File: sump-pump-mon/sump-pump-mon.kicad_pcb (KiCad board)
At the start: 2 copper layers, 36 parts, among them J1 Main Input, J2 Wall Power, J3 Battery, J4 Conn_01x06_Pin, J5 Aux Input, SW3 MODE, SW4 POWER, U1 L7805, U2 4N25, U3 4N25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

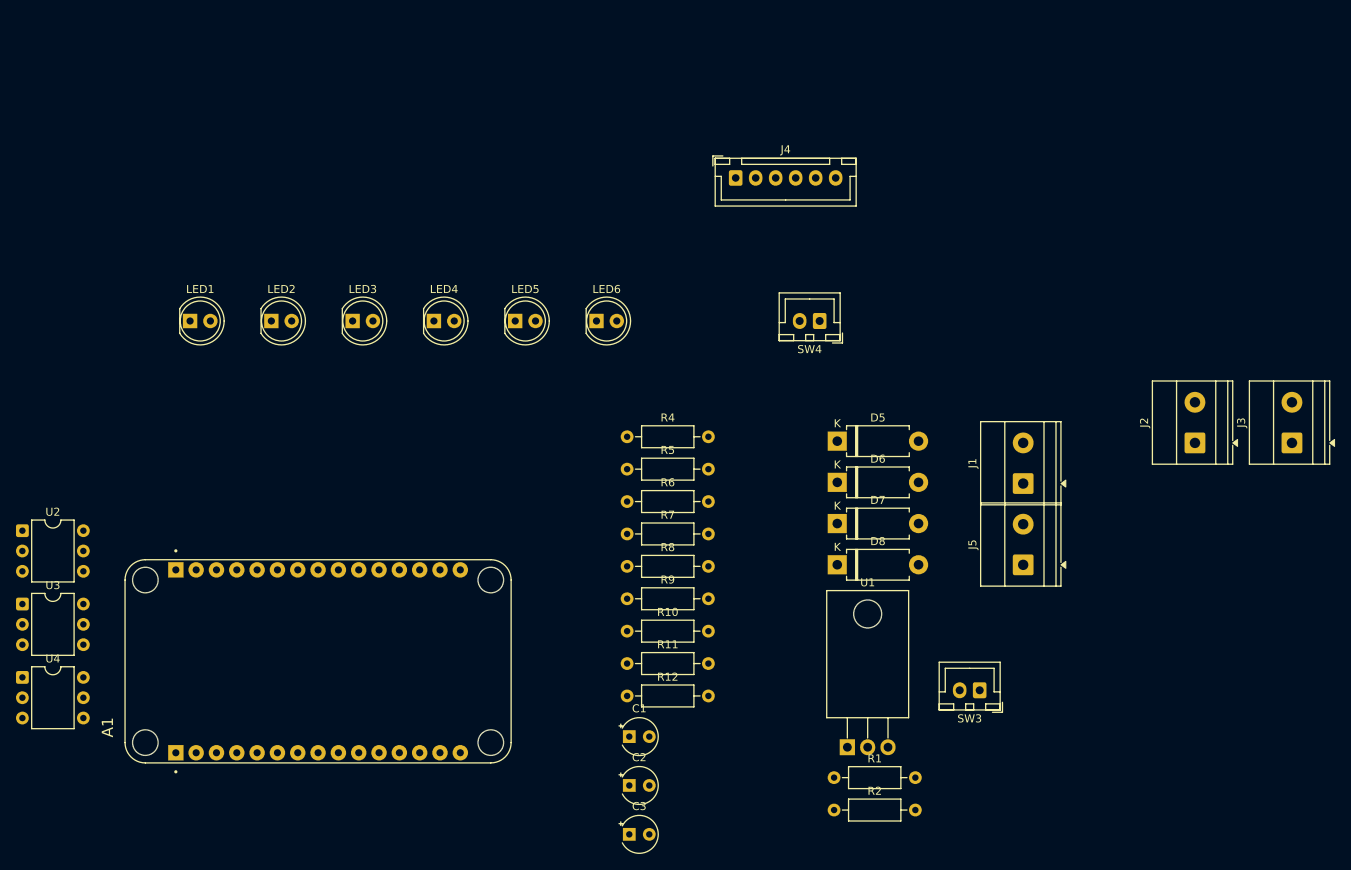
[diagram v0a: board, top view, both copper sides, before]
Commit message: Rough parts placement and partial routing
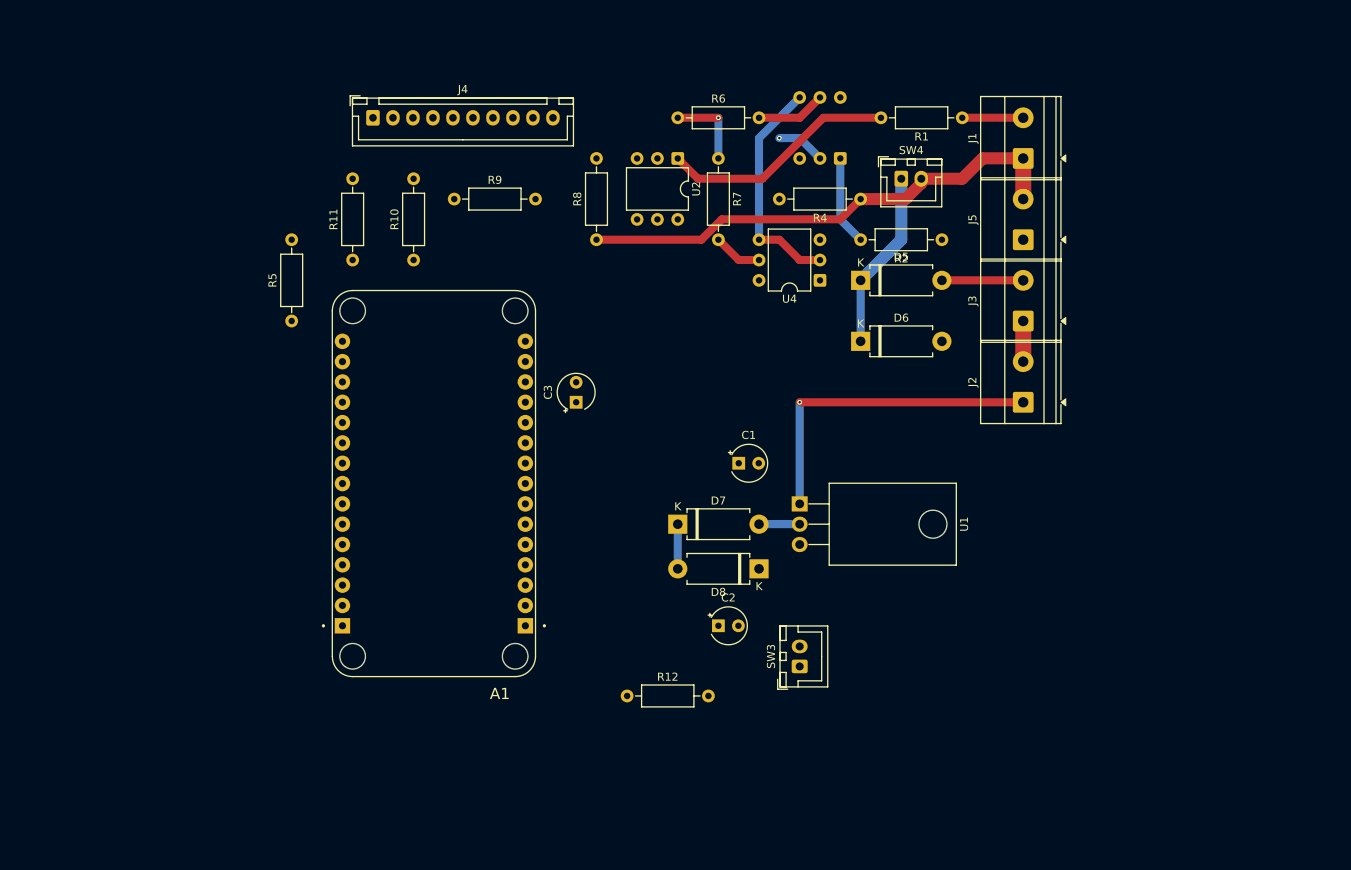
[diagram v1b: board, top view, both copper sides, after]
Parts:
- removed LED1: LED_POWER, LED_THT:LED_D5.0mm
- removed LED2: LED_MAIN, LED_THT:LED_D5.0mm
- removed LED3: LED_AUX, LED_THT:LED_D5.0mm
- removed LED4: GREEN, LED_THT:LED_D5.0mm
- removed LED5: YELLOW, LED_THT:LED_D5.0mm
- removed LED6: LED_MODE, LED_THT:LED_D5.0mm
- J4: footprint Connector_JST:JST_XH_B6B-XH-A_1x06_P2.50mm_Vertical -> Connector_JST:JST_XH_B10B-XH-A_1x10_P2.50mm_Vertical
- U3: moved to B.Cu
- moved U3 116.4 mm to (195.6, 35.6), turned to 90 degrees
- moved U4 111.4 mm to (193.0, 50.8), turned to 180 degrees
- moved U2 94.2 mm to (175.3, 35.6), turned to -90 degrees
- moved R1 84.0 mm to (210.8, 30.5), turned to 180 degrees
- moved R2 72.6 mm to (208.3, 45.7), turned to 180 degrees
- moved R11 61.0 mm to (134.6, 48.3), turned to 90 degrees
- moved R9 54.4 mm to (147.3, 40.6)
- moved C3 54.4 mm to (162.6, 66.0), turned to 90 degrees
- moved R10 53.5 mm to (142.2, 48.3), turned to 90 degrees
- moved R6 48.4 mm to (175.3, 30.5)
- moved R7 48.3 mm to (180.3, 35.6), turned to -90 degrees
- moved J4 46.0 mm to (137.2, 30.5)
- moved R5 45.8 mm to (127.0, 55.9), turned to 90 degrees
- moved R4 41.7 mm to (198.1, 40.6), turned to 180 degrees
- moved R8 41.0 mm to (165.1, 45.7), turned to 90 degrees
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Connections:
- C1 pad 1: Net-(J2-Pin_2) -> Net-(J2-Pin_1)
- J2 pad 1: GND -> Net-(J2-Pin_1)
- J2 pad 2: Net-(J2-Pin_2) -> GND
- J4 pad 6: GND -> LED_AUX
- R1 pad 2: Net-(LED2-A) -> Net-(R1-Pad2)
- R2 pad 2: Net-(LED3-A) -> Net-(R2-Pad2)
- U1 pad 1: Net-(J2-Pin_2) -> Net-(J2-Pin_1)
- U2 pad 1: Net-(LED2-K) -> Net-(R1-Pad2)
- U2 pad 2: GND -> LED_MAIN
- U3 pad 1: Net-(LED3-K) -> Net-(R2-Pad2)
- U3 pad 2: GND -> LED_AUX
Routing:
- net Vin: track 0.00 -> 63.0 mm
- net Net-(J2-Pin_1): track 0.00 -> 40.6 mm, vias 0 -> 1
- net GND: track 0.00 -> 33.6 mm
- net Net-(R1-Pad2): track 0.00 -> 29.6 mm
- net Net-(D5-K): track 0.00 -> 22.4 mm
- net Net-(R2-Pad2): track 0.00 -> 11.2 mm
- net +3.3V: track 0.00 -> 10.2 mm, vias 0 -> 1
- net Net-(D5-A): track 0.00 -> 10.2 mm
- net Aux_Input: track 0.00 -> 8.67 mm
- net Net-(J1-Pin_2): track 0.00 -> 7.62 mm
- net Power_Failure: track 0.00 -> 6.13 mm
- net LED_AUX: track 0.00 -> 6.13 mm, vias 0 -> 1
- net Net-(D7-K): track 0.00 -> 5.58 mm
- net Net-(D7-A): track 0.00 -> 5.08 mm

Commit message: Routing complete
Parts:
- added H1: MountingHole, MountingHole:MountingHole_3.7mm, F.Cu at (218.4, 22.9)
- added H2: MountingHole, MountingHole:MountingHole_3.7mm, F.Cu at (218.4, 73.7)
- added H3: MountingHole, MountingHole:MountingHole_3.7mm, F.Cu at (116.4, 22.9)
- added H4: MountingHole, MountingHole:MountingHole_3.7mm, F.Cu at (116.4, 73.7)
- added J6: I2C, Connector_JST:JST_XH_B2B-XH-A_1x02_P2.50mm_Vertical, F.Cu at (135.9, 24.1)
- added R13: 2.7k, Resistor_THT:R_Axial_DIN0207_L6.3mm_D2.5mm_P10.16mm_Horizontal, F.Cu at (153.7, 21.6)
- added R14: 2.7k, Resistor_THT:R_Axial_DIN0207_L6.3mm_D2.5mm_P10.16mm_Horizontal, F.Cu at (116.8, 50.8)
- J2, J3: footprint TerminalBlock_Phoenix:TerminalBlock_Phoenix_MKDS-1,5-2-5.08_1x02_P5.08mm_Horizontal -> Connector_JST:JST_XH_B2B-XH-A_1x02_P2.50mm_Vertical
- J4: value Conn_01x06_Pin -> Display_Conn; footprint Connector_JST:JST_XH_B10B-XH-A_1x10_P2.50mm_Vertical -> Connector_JST:JST_XH_B12B-XH-A_1x12_P2.50mm_Vertical
- U1: footprint Package_TO_SOT_THT:TO-220-3_Horizontal_TabDown -> Package_TO_SOT_THT:TO-220-3_Vertical
- U3: moved to F.Cu
- moved SW3 51.4 mm to (172.7, 50.8), turned to 0 degrees
- moved C3 46.4 mm to (116.8, 58.4), turned to 0 degrees
- moved J4 36.8 mm to (163.8, 55.9), turned to 90 degrees
- moved R12 35.7 mm to (152.4, 71.1), turned to 90 degrees
- moved R5 32.1 mm to (157.5, 66.0)
- moved C2 31.8 mm to (195.6, 66.0), turned to 90 degrees
- moved D8 28.9 mm to (190.5, 58.4)
- moved A1 25.0 mm to (134.6, 53.3), turned to 0 degrees
- moved C1 21.7 mm to (203.2, 66.0), turned to 90 degrees
- moved R11 20.5 mm to (152.4, 58.4)
- moved D7 16.1 mm to (180.3, 66.0)
- moved U1 14.8 mm to (203.2, 71.1), turned to 180 degrees
- moved R8 10.8 mm to (157.5, 53.3)
- moved R10 10.5 mm to (152.4, 45.7)
- moved R9 10.2 mm to (157.5, 40.6), turned to 90 degrees
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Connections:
- net LED_POWER renamed LED_6V
- A1 pad J1_11: Net-(A1A-3V3) -> +3.3V
- A1 pad J2_4: unconnected-(A1B-D3-PadJ2_4) -> Net-(A1B-D3)
- A1 pad J2_5: unconnected-(A1B-D4-PadJ2_5) -> Net-(A1B-D4)
- C3 pad 1: Net-(A1A-3V3) -> +3.3V
- R10 pad 1: Net-(A1B-D2) -> Net-(A1B-D4)
- R9 pad 1: Net-(A1B-D1) -> Net-(A1B-D3)
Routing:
- net GND: track 33.6 -> 204.2 mm, vias 0 -> 1
- net +3.3V: track 10.2 -> 139.8 mm
- net Vin: track 63.0 -> 191.0 mm, vias 0 -> 2
- net Power_Failure: track 6.13 -> 69.4 mm, vias 0 -> 2
- net Aux_Input: track 8.67 -> 66.8 mm, vias 0 -> 1
- net Net-(A1B-D2): track 0.00 -> 53.3 mm
- net Mode: track 0.00 -> 46.8 mm, vias 0 -> 1
- net LED_AUX: track 6.13 -> 46.4 mm
- net Main_Input: track 0.00 -> 37.9 mm, vias 0 -> 1
- net Net-(A1B-D1): track 0.00 -> 27.3 mm
- net Net-(J2-Pin_1): track 40.6 -> 16.5 mm, vias 1 -> 0
- net LED_BLUE: track 0.00 -> 23.8 mm, vias 0 -> 1
- net Net-(D6-A): track 0.00 -> 22.0 mm
- net LED_YELLOW: track 0.00 -> 13.6 mm
- net Net-(A1B-D3): track 0.00 -> 12.5 mm
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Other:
- board outline added: 111.8 x 61 mm
- board text added: "+"
- board text added: "-"
- board text added: "AUX"
- board text added: "BATT"
- board text added: "MAIN"
- board text added: "SCL"
- board text added: "SDA"
- board text added: "WALL"

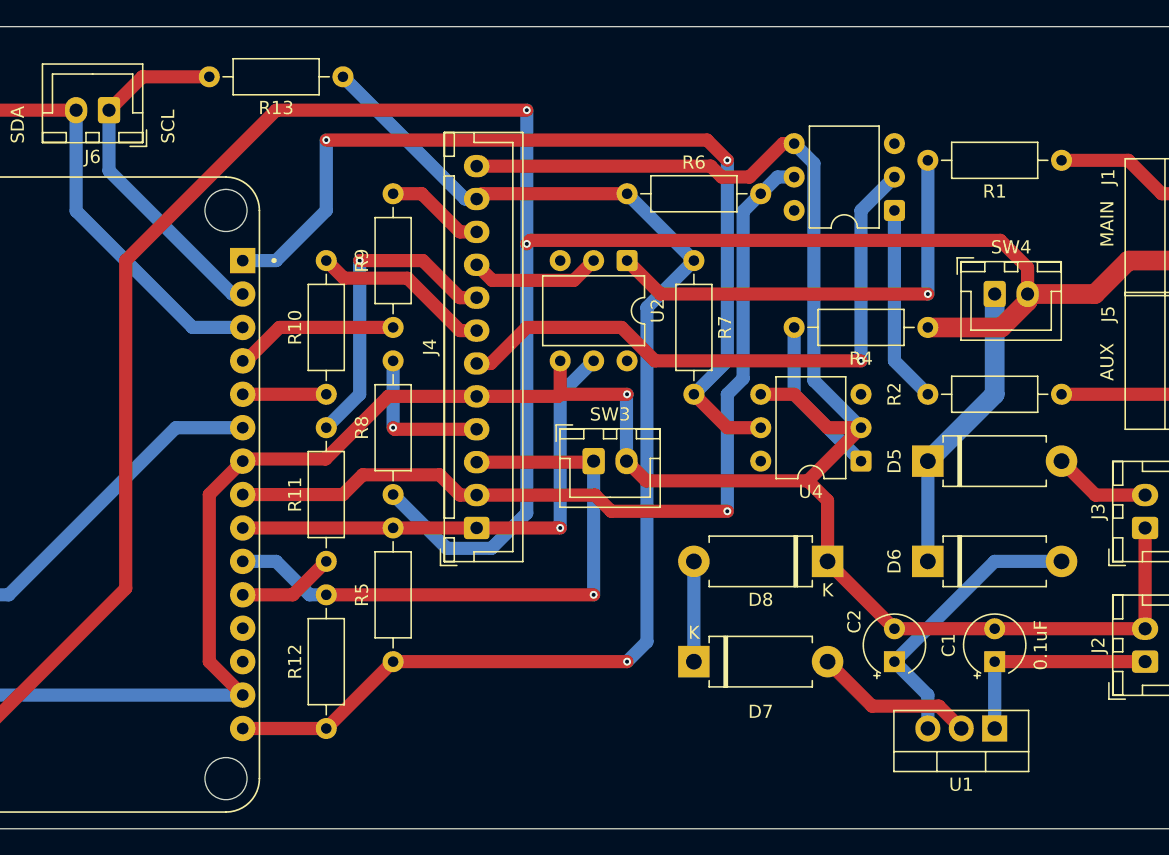
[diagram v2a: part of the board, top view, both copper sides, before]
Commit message: add values to silkscreen
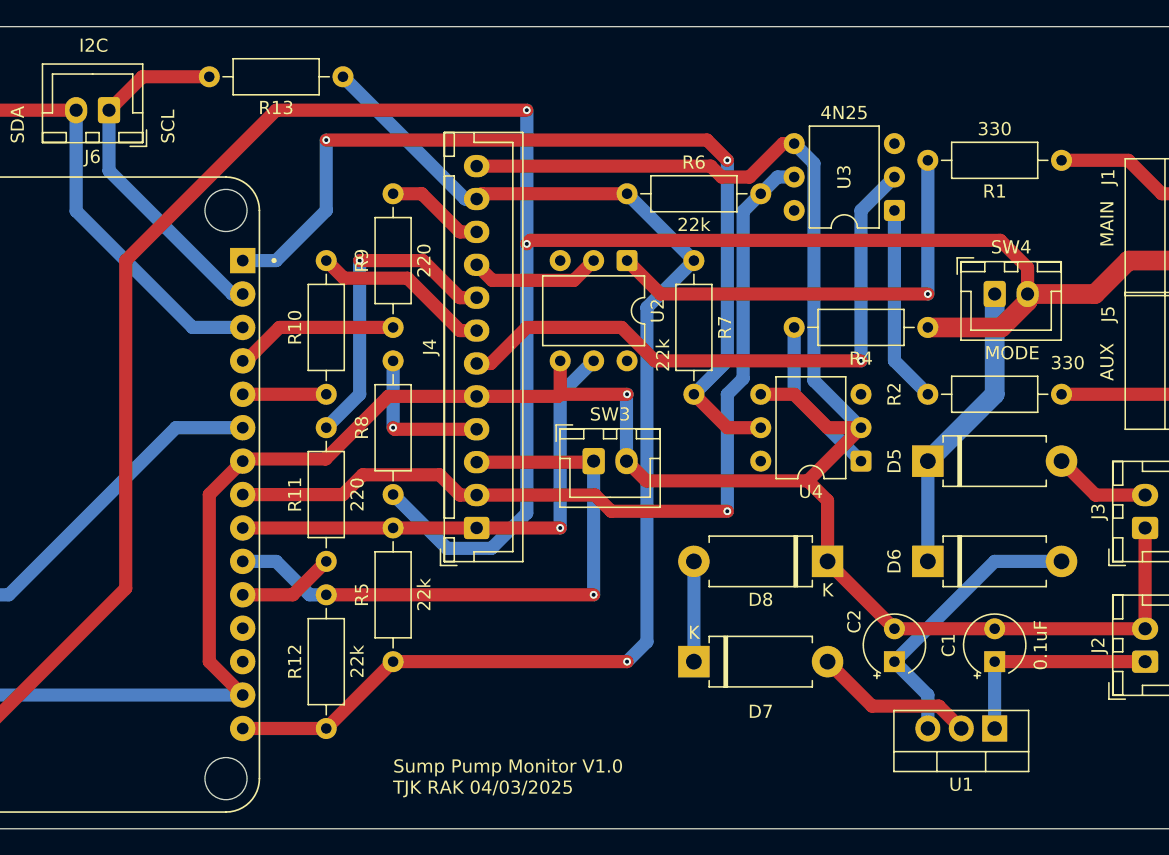
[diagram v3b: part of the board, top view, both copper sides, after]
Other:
- board text added: "I2C"
- board text added: "MODE"
- board text added: "Sump Pump Monitor V1.0 TJK RAK 04/03/2025"
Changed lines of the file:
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@@
 			(outputformat 1)
 			(mirror no)
-			(drillshape 1)
+			(drillshape 0)
 			(scaleselection 1)
-			(outputdirectory "")
+			(outputdirectory "gerbers")
 		)
 	)
@@
 		)
 		(property "Value" "330"
-			(at 5.08 2.37 0)
-			(layer "F.Fab")
+			(at -0.47 2.37 0)
+			(layer "F.SilkS")
 			(effects
 				(font
@@
 		)
 		(property "Value" "22k"
-			(at 5.08 2.37 90)
-			(layer "F.Fab")
+			(at 7.19 2.34 90)
+			(layer "F.SilkS")
 			(effects
 				(font
@@
 		(property "Value" "22k"
 			(at 5.08 2.37 0)
-			(layer "F.Fab")
+			(layer "F.SilkS")
 			(effects
 				(font
@@
 		(property "Value" "220"
 			(at 5.08 2.37 90)
-			(layer "F.Fab")
+			(layer "F.SilkS")
 			(effects
 				(font
@@
 		(property "Value" "4N25"
 			(at 3.81 7.41 0)
-			(layer "F.Fab")
+			(layer "F.SilkS")
 			(effects
 				(font
@@
 		(fp_text user "${REFERENCE}"
 			(at 3.81 2.54 90)
-			(layer "F.Fab")
+			(layer "F.SilkS")
 			(effects
 				(font
@@
 		(property "Value" "220"
 			(at 5.08 2.37 90)
-			(layer "F.Fab")
+			(layer "F.SilkS")
 			(effects
 				(font
@@
 		(property "Value" "22k"
 			(at 5.08 2.37 90)
-			(layer "F.Fab")
+			(layer "F.SilkS")
 			(effects
 				(font
@@
 		(property "Value" "330"
 			(at 5.08 2.37 0)
-			(layer "F.Fab")
+			(layer "F.SilkS")
 			(effects
 				(font
@@
 		(property "Value" "22k"
 			(at 5.08 2.37 90)
-			(layer "F.Fab")
+			(layer "F.SilkS")
 			(effects
 				(font
@@
 		)
 	)
+	(gr_text "Sump Pump Monitor V1.0\nTJK RAK 04/03/2025"
+		(at 157.48 76.2 0)
+		(layer "F.SilkS")
+		(effects
+			(font
+				(size 1 1)
+				(thickness 0.1)
+			)
+			(justify left bottom)
+		)
+	)
 	(gr_text "-\n"
 		(at 220.726 62.23 90)
@@
 		(layer "F.SilkS")
 		(effects
+			(font
+				(size 1 1)
+				(thickness 0.1)
+			)
+			(justify left bottom)
+		)
+	)
+	(gr_text "I2C"
+		(at 133.604 19.812 0)
+		(layer "F.SilkS")
+		(effects
+			(font
+				(size 1 1)
+				(thickness 0.1)
+			)
+			(justify left bottom)
+		)
+	)
+	(gr_text "MODE"
+		(at 202.438 43.18 0)
+		(layer "F.SilkS")
+		(effects
